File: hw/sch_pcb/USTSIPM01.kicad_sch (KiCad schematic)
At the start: 39 parts, among them J4 HEADER_2x01_PARALLEL, J5 HEADER_2x01_PARALLEL, J6 HEADER_2x01_PARALLEL, J8 HEADER_2x01_PARALLEL, J9 HEADER_2x01_PARALLEL, U1 MICROFC-60035-SMT-TR(1), U2 OPA836IDB, U3 MAX5026

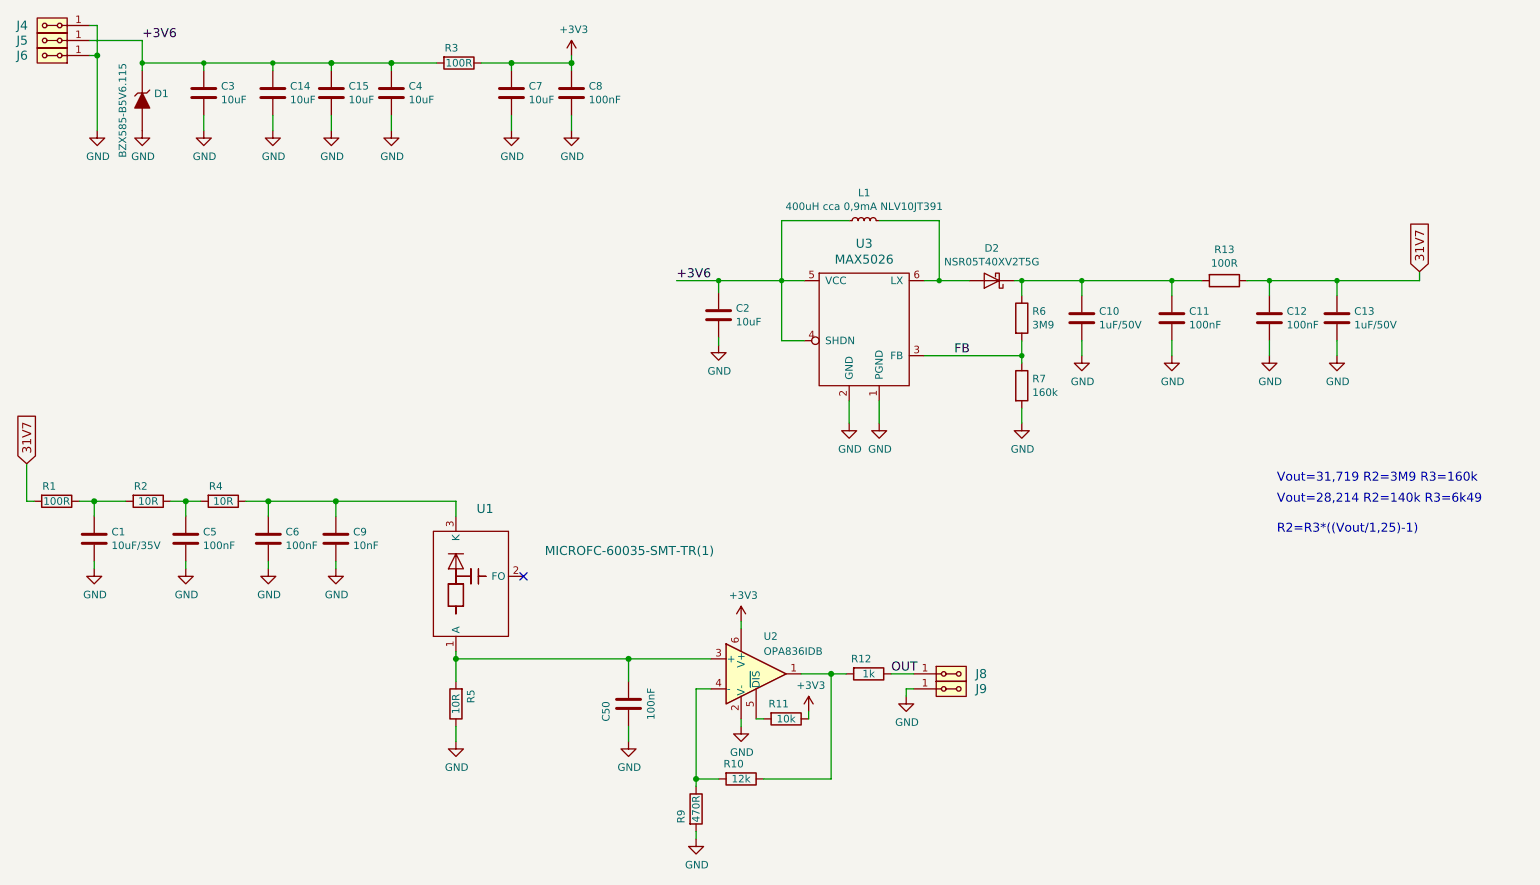
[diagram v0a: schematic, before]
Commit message: Align schematics symbols to grid. Update PCB from schematic. Improve silkscreen. Move PCB to center of the page.
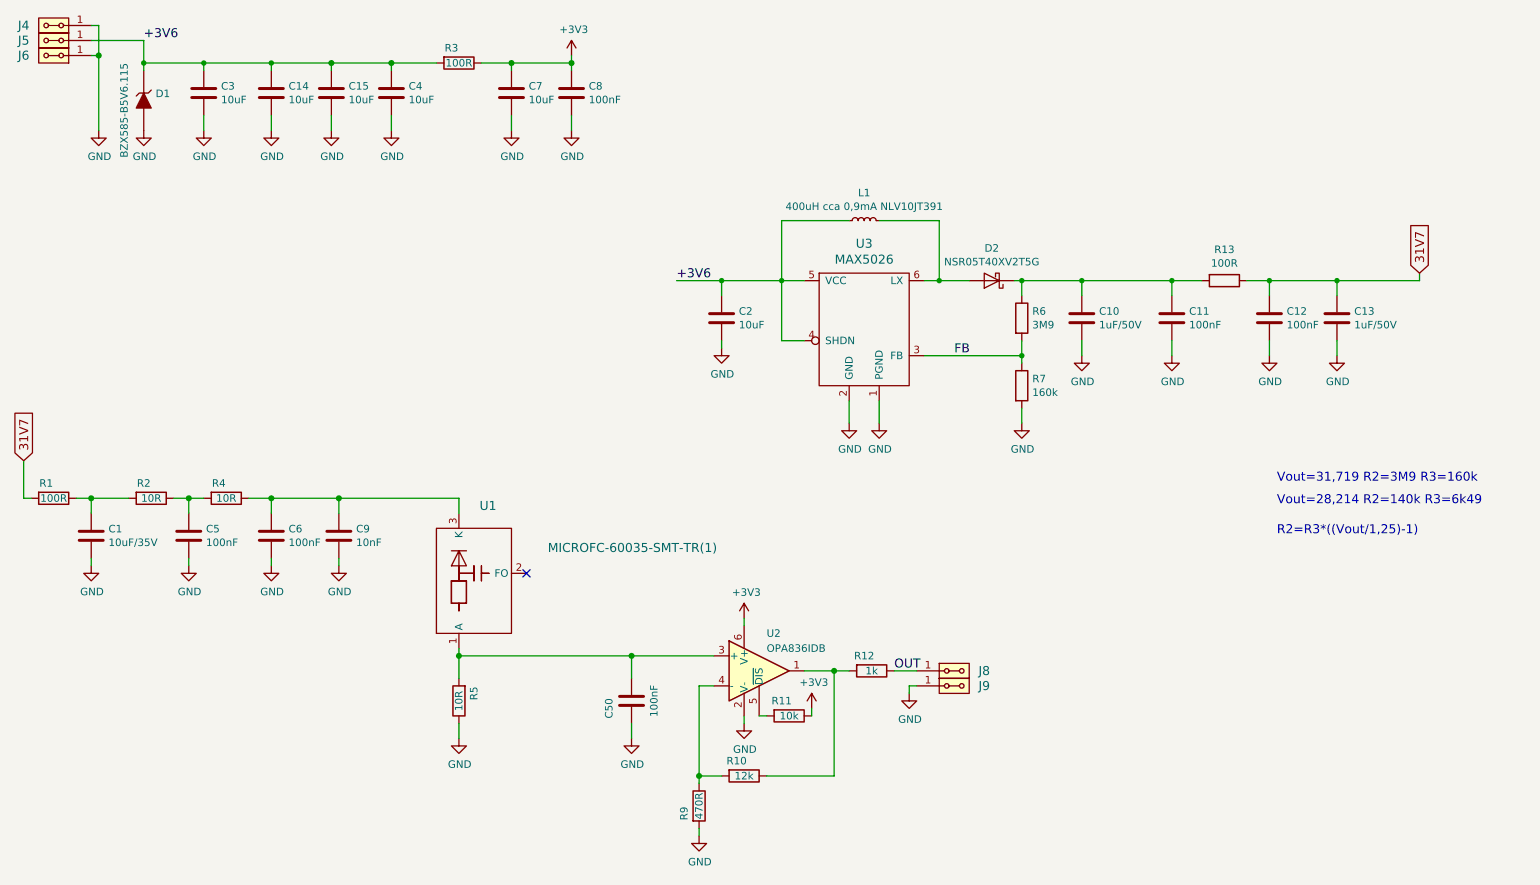
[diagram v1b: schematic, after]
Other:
- moved on the sheet: C1, C2, C5, C50, C6, C9, J8, J9, R1, R10, R11, R12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
